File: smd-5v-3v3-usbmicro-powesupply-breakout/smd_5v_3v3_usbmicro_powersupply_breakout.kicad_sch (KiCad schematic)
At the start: 13 parts, among them J1 USB_B_Micro, J2 THT 5V Jumper, J3 THT 3V3 Jumper, J4 SMD 5V Pad, J5 SMD 3V3 Pad, U1 LMS1585AIS-3.3

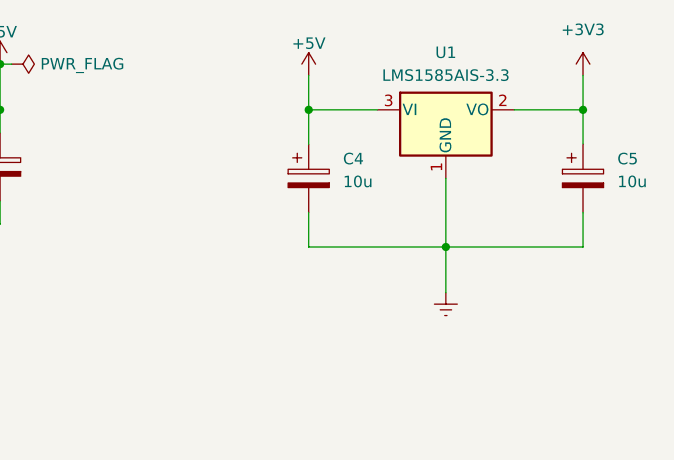
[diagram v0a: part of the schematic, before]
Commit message: v03 update (remove LDO input capacitor)
- LDO input capacitor isn't required as the pi-filter should reduce the
  ripples on the VBUS line giving us a "cleaner" 5V line therefore
  another input capacitor on the LDO isn't required (as there shouldn't
  be excessive rippling/noise)
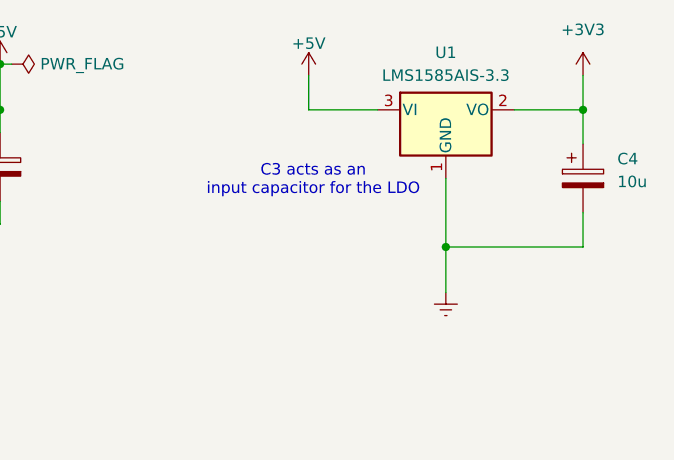
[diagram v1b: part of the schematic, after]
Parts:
- removed C4: 10u, Capacitor_SMD:CP_Elec_4x4.5, symbol Device:C_Polarized
- renumbered C5 to C4
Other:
- note added: "C3 acts as an input capacitor for the LDO"
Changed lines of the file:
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@@
 		(title "5V & 3V3 USB Micro Power Supply Breakout Board")
 		(date "2025-02-11")
-		(rev "v02")
+		(rev "v03")
 		(comment 3 "With filtering and ESD protection")
 		(comment 4 "Simple 5V & 3V3 power supply from USB micro input (VBUS)")
@@
 		(color 0 0 0 0)
 	)
-	(junction
-		(at 135.89 52.07)
-		(diameter 0)
-		(color 0 0 0 0)
-	)
 	(no_connect
 		(at 57.15 62.23)
@@
 	(wire
 		(pts
-			(xy 135.89 63.5) (xy 135.89 67.31)
-		)
-		(stroke
-			(width 0)
-			(type default)
-		)
-	)
-	(wire
-		(pts
 			(xy 21.59 111.76) (xy 27.94 111.76)
 		)
@@
 	(wire
 		(pts
-			(xy 135.89 52.07) (xy 135.89 55.88)
-		)
-		(stroke
-			(width 0)
-			(type default)
-		)
-	)
-	(wire
-		(pts
 			(xy 87.63 64.77) (xy 87.63 67.31)
 		)
@@
 	(wire
 		(pts
-			(xy 135.89 67.31) (xy 151.13 67.31)
-		)
-		(stroke
-			(width 0)
-			(type default)
-		)
-	)
-	(wire
-		(pts
 			(xy 101.6 62.23) (xy 101.6 64.77)
 		)
@@
 		)
 	)
-	(symbol
-		(lib_id "Device:C_Polarized")
-		(at 135.89 59.69 0)
-		(unit 1)
-		(exclude_from_sim no)
-		(in_bom yes)
-		(on_board yes)
-		(dnp no)
-		(fields_autoplaced yes)
-		(property "Reference" "C4"
-			(at 139.7 57.5309 0)
-			(effects
-				(font
-					(size 1.27 1.27)
-				)
-				(justify left)
-			)
-		)
-		(property "Value" "10u"
-			(at 139.7 60.0709 0)
-			(effects
-				(font
-					(size 1.27 1.27)
-				)
-				(justify left)
-			)
-		)
-		(property "Footprint" "Capacitor_SMD:CP_Elec_4x4.5"
-			(at 136.8552 63.5 0)
-			(effects
-				(font
-					(size 1.27 1.27)
-				)
-				(hide yes)
-			)
-		)
-		(property "Datasheet" "~"
-			(at 135.89 59.69 0)
-			(effects
-				(font
-					(size 1.27 1.27)
-				)
-				(hide yes)
-			)
-		)
-		(property "Description" "Polarized capacitor"
-			(at 135.89 59.69 0)
-			(effects
-				(font
-					(size 1.27 1.27)
-				)
-				(hide yes)
-			)
-		)
-		(pin "1"
-		)
-		(pin "2"
-		)
-		(instances
-			(project "smd_5v_3v3_usbmicro_powersupply_breakout"
-				(path "/7adebb7f-893e-483f-8b11-729f4eaf6a9d"
-					(reference "C4")
-					(unit 1)
-				)
+	(text "C3 acts as an \ninput capacitor for the LDO"
+		(exclude_from_sim no)
+		(at 136.398 59.944 0)
+		(effects
+			(font
+				(size 1.27 1.27)
 			)
 		)
@@
 		(dnp no)
 		(fields_autoplaced yes)
-		(property "Reference" "C5"
+		(property "Reference" "C4"
 			(at 170.18 57.5309 0)
 			(effects
@@
 			(project "smd_5v_3v3_usbmicro_powersupply_breakout"
 				(path "/7adebb7f-893e-483f-8b11-729f4eaf6a9d"
-					(reference "C5")
-					(unit 1)
-				)
+					(reference "C4")
+					(unit 1)
+				)
